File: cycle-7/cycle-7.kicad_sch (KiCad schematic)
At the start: 176 parts, among them J1 Conn_01x06_MountingPin, J2 Conn_01x04_Pin, J3 Conn_01x02_Pin, SW1 SW_Push, U1 XC6206PxxxMR, U2 STM32F401RCTx, Y1 12MHz

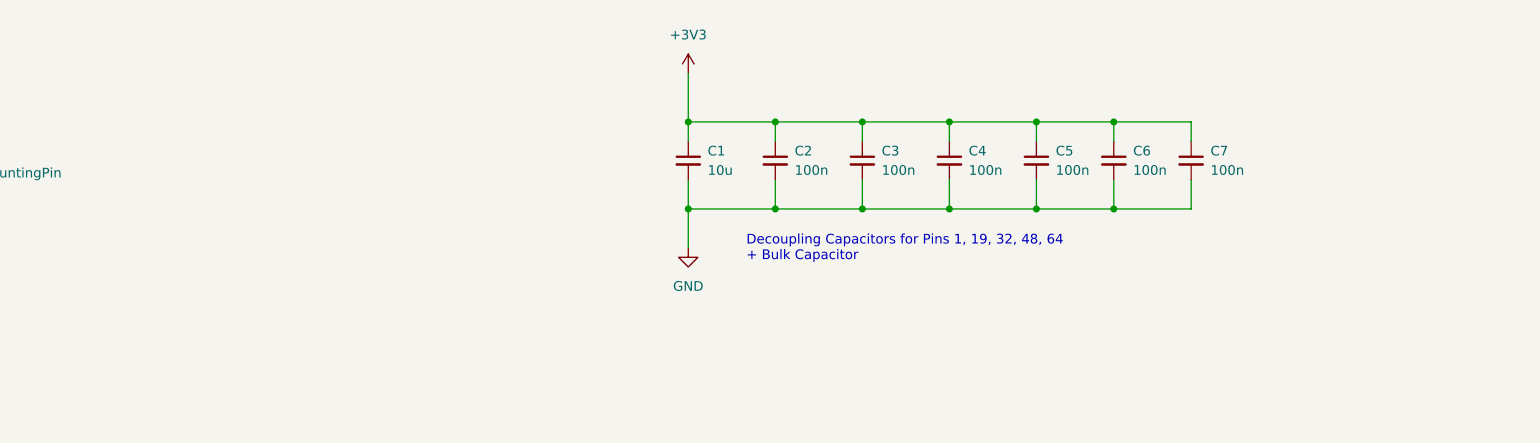
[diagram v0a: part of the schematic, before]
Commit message: fixed layout, added gnd plane stitching
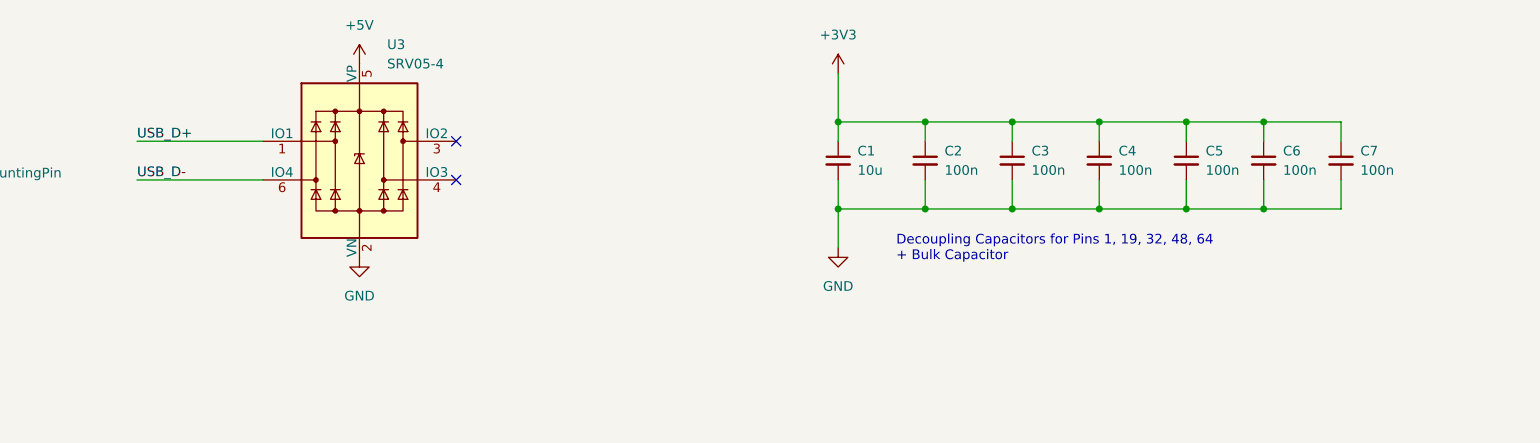
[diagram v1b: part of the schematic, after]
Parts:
- added U3: SRV05-4, PCM_marbastlib-various:SOT-23-6-routable, symbol PCM_marbastlib-various:SRV05-4
- C1, C10, C11, C12, C13, C2, C3, C4, C5, C6, C7, C8, C9: footprint Capacitor_SMD:C_0402_1005Metric -> Capacitor_SMD:C_0603_1608Metric
- D74: footprint LED_SMD:LED_RGB_1210 -> lib-zegonix:SK6812MINI-E_3.2x2.8_reverse_mount
- R1, R2, R3: footprint Resistor_SMD:R_0402_1005Metric -> Resistor_SMD:R_0603_1608Metric
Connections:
- net +5V: now also U3.5 (VP)
- net GND: now also U3.2 (VN)
- net USB_D+: now also U3.1 (IO1)
- net USB_D-: now also U3.6 (IO4)
- no-connect marks 25 -> 27
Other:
- moved on the sheet: C1, C2, C3, C4, C5, C6, C7

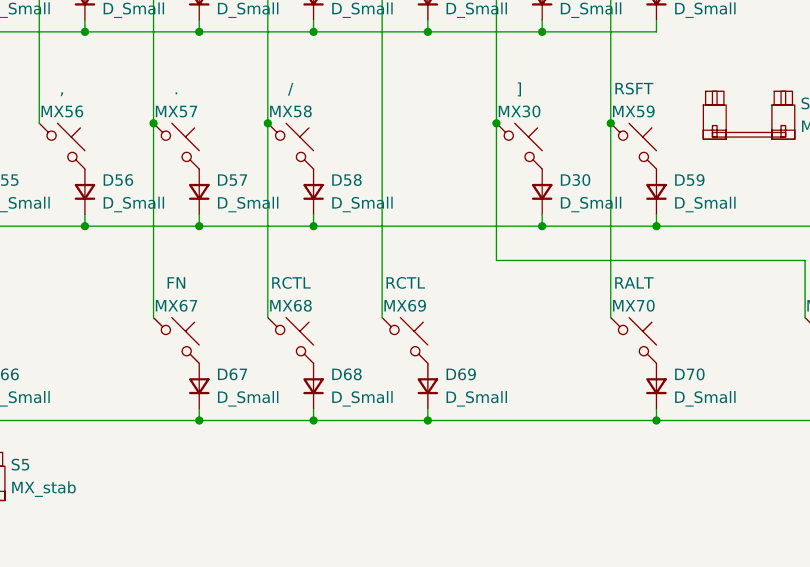
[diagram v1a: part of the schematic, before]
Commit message: added a kicad project for the plate added a kicad project for the daughter board
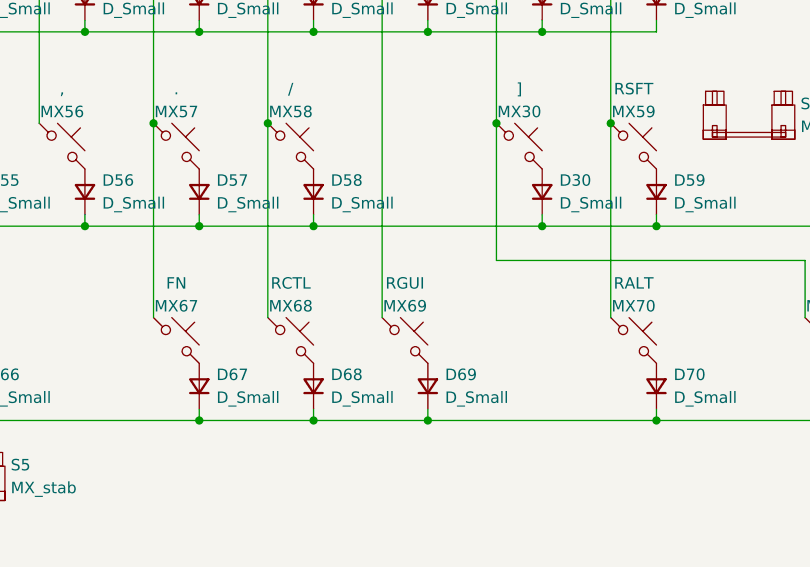
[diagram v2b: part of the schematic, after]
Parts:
- MX69: Key RCTL -> RGUI
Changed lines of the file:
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@@
       (effects (font (size 1.27 1.27)) hide)
     )
-    (property "Key" "RCTL" (at 314.96 195.58 0)
+    (property "Key" "RGUI" (at 314.96 195.58 0)
       (effects (font (size 1.27 1.27)))
     )

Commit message: implemented newest findings from prototype and updated to kicad 8
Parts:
- added R4, R5: 10k, Resistor_SMD:R_0603_1608Metric, symbol Device:R_Small
- C11: value 100n -> 4.7u
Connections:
- net +3V3: now also J3.1 (Pin_1)
- net GND: now also R4.1, R5.1; no longer J3.2 (Pin_2)
- net BOOT1: now reaches U2.28 (PB2)
- net BOOT1: now also R4.2
- net BOOTSEL renamed BOOT0
- net BOOT0: now also J3.2 (Pin_2), R5.2; no longer J3.1 (Pin_1)
- no-connect marks 27 -> 26
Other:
- note removed: "PB2 has alternate Function BOOT1"
- moved on the sheet: C1, C2, C3, C4, C5, C6, C7, D74, J3

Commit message: minor fixes
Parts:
- C11: value 4.7u -> 100n
- renumbered D14 to D13, D15 to D14, D16 to D15, D17 to D16, D18 to D17, D19 to D18, D20 to D19, D21 to D20, D22 to D21, D23 to D22, D24 to D23, D25 to D24, D26 to D25, D27 to D26, D28 to D27, D29 to D28, D31 to D29, D32 to D30, D33 to D31, D34 to D32, D35 to D33, D36 to D34, D37 to D35, D38 to D36, D39 to D37, D40 to D38, D41 to D39, D42 to D40, D43 to D41, D44 to D42, D45 to D43, D46 to D44, D13 to D45, D47 to D46, D48 to D47, D49 to D48, D50 to D49, D51 to D50, D52 to D51, D53 to D52, D54 to D53, D55 to D54, D56 to D55, D57 to D56, D58 to D57, D30 to D58, J3 to J2, J2 to J3, MX14 to MX13, MX15 to MX14, MX16 to MX15, MX17 to MX16, MX18 to MX17, MX19 to MX18, MX20 to MX19, MX21 to MX20, MX22 to MX21, MX23 to MX22, MX24 to MX23, MX25 to MX24, MX26 to MX25, MX27 to MX26, MX28 to MX27, MX29 to MX28, MX31 to MX29, MX32 to MX30, MX33 to MX31, MX34 to MX32, MX35 to MX33, MX36 to MX34, MX37 to MX35, MX38 to MX36, MX39 to MX37, MX40 to MX38, MX41 to MX39, MX42 to MX40, MX43 to MX41, MX44 to MX42, MX45 to MX43, MX46 to MX44, MX13 to MX45, MX47 to MX46, MX48 to MX47, MX49 to MX48, MX50 to MX49, MX51 to MX50, MX52 to MX51, MX53 to MX52, MX54 to MX53, MX55 to MX54, MX56 to MX55, MX57 to MX56, MX58 to MX57, MX30 to MX58, R5 to R4, R4 to R5, S6 to S5, S5 to S6, U3 to U2, U2 to U3

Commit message: added a readme, fixed kicad update mess..
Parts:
- C10: value 100n -> 10n
- J1: footprint Connector_JST:JST_SHL_SM06B-SHLS-TF_1x06-1MP_P1.00mm_Horizontal -> Connector_JST:JST_SH_SM06B-SRSS-TB_1x06-1MP_P1.00mm_Horizontal
- R1, R2: value 27 -> 0
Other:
- note added: "Decoupling Capacitors for Pins 1, 13, 19, 32, 48, 64 + Bulk Capacitor"
- note added: "the F401 chips have the resistors embedded"
- note removed: "Decoupling Capacitors for Pins 1, 19, 32, 48, 64 + Bulk Capacitor"
- moved on the sheet: C10, SW1
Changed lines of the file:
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@@
 	)
 	(junction
-		(at 54.61 49.53)
+		(at 54.61 45.72)
 		(diameter 0)
 		(color 0 0 0 0)
@@
 	(wire
 		(pts
-			(xy 39.37 58.42) (xy 39.37 60.96)
+			(xy 39.37 57.15) (xy 39.37 60.96)
 		)
 		(stroke
@@
 	(wire
 		(pts
-			(xy 39.37 49.53) (xy 54.61 49.53)
+			(xy 39.37 45.72) (xy 54.61 45.72)
 		)
 		(stroke
@@
 	(wire
 		(pts
-			(xy 54.61 49.53) (xy 54.61 50.8)
+			(xy 54.61 45.72) (xy 54.61 49.53)
 		)
 		(stroke
@@
 	(wire
 		(pts
-			(xy 54.61 49.53) (xy 77.47 49.53)
+			(xy 54.61 45.72) (xy 77.47 45.72)
 		)
 		(stroke
@@
 	(wire
 		(pts
+			(xy 54.61 59.69) (xy 54.61 60.96)
+		)
+		(stroke
+			(width 0)
+			(type default)
+		)
+	)
+	(wire
+		(pts
 			(xy 228.6 167.64) (xy 228.6 166.37)
 		)
@@
 	(wire
 		(pts
-			(xy 39.37 49.53) (xy 39.37 53.34)
+			(xy 39.37 45.72) (xy 39.37 52.07)
 		)
 		(stroke
@@
 		)
 	)
-	(text "Decoupling Capacitors for Pins 1, 19, 32, 48, 64\n+ Bulk Capacitor"
+	(text "Decoupling Capacitors for Pins 1, 13, 19, 32, 48, 64\n+ Bulk Capacitor"
 		(exclude_from_sim no)
 		(at 300.355 62.865 0)
@@
 		)
 	)
+	(text "the F401 chips have the resistors embedded"
+		(exclude_from_sim no)
+		(at 118.364 114.3 0)
+		(effects
+			(font
+				(size 1.27 1.27)
+			)
+		)
+	)
 	(label "COL5"
 		(at 236.22 93.98 270)
@@
 	)
 	(label "nRESET"
-		(at 77.47 49.53 180)
+		(at 77.47 45.72 180)
 		(fields_autoplaced yes)
 		(effects
@@
 	(symbol
 		(lib_id "Switch:SW_Push")
-		(at 54.61 55.88 90)
+		(at 54.61 54.61 90)
 		(unit 1)
 		(exclude_from_sim no)
@@
 		(fields_autoplaced yes)
 		(property "Reference" "SW1"
-			(at 56.515 54.61 90)
+			(at 56.515 53.34 90)
 			(effects
 				(font
@@
 		)
 		(property "Value" "SW_Push"
-			(at 56.515 57.15 90)
+			(at 56.515 55.88 90)
 			(effects
 				(font
@@
 		)
 		(property "Footprint" "Button_Switch_SMD:SW_SPST_TL3342"
-			(at 49.53 55.88 0)
+			(at 49.53 54.61 0)
 			(effects
 				(font
@@
 		)
 		(property "Datasheet" "~"
-			(at 49.53 55.88 0)
+			(at 49.53 54.61 0)
 			(effects
 				(font
@@
 		)
 		(property "Description" ""
-			(at 54.61 55.88 0)
+			(at 54.61 54.61 0)
 			(effects
 				(font
@@
 	(symbol
 		(lib_id "Device:C_Small")
-		(at 39.37 55.88 0)
+		(at 39.37 54.61 0)
 		(unit 1)
 		(exclude_from_sim no)
@@
 		(fields_autoplaced yes)
 		(property "Reference" "C10"
-			(at 41.91 54.6163 0)
+			(at 41.91 53.3462 0)
 			(effects
 				(font
@@
 			)
 		)
-		(property "Value" "100n"
-			(at 41.91 57.1563 0)
+		(property "Value" "10n"
+			(at 41.91 55.8862 0)
 			(effects
 				(font
@@
 		)
 		(property "Footprint" "Capacitor_SMD:C_0603_1608Metric"
-			(at 39.37 55.88 0)
+			(at 39.37 54.61 0)
 			(effects
 				(font
@@
 		)
 		(property "Datasheet" "~"
-			(at 39.37 55.88 0)
+			(at 39.37 54.61 0)
 			(effects
 				(font
@@
 		)
 		(property "Description" ""
-			(at 39.37 55.88 0)
+			(at 39.37 54.61 0)
 			(effects
 				(font
@@
 			)
 		)
-		(property "Value" "27"
+		(property "Value" "0"
 			(at 104.775 116.84 90)
 			(effects
@@
 			)
 		)
-		(property "Footprint" "Connector_JST:JST_SHL_SM06B-SHLS-TF_1x06-1MP_P1.00mm_Horizontal"
+		(property "Footprint" "Connector_JST:JST_SH_SM06B-SRSS-TB_1x06-1MP_P1.00mm_Horizontal"
 			(at 165.1 48.26 0)
 			(effects
@@
 			)
 		)
-		(property "Value" "27"
+		(property "Value" "0"
 			(at 104.775 119.38 90)
 			(effects

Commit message: .
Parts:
- added C14: 100n, Capacitor_SMD:C_0603_1608Metric, symbol Device:C_Small
- added R6: 1k, symbol Device:R_Small
- C10: value 10n -> 100n
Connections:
- net +5V: now also C14.1
- net GND: now also C14.2
- net USB_D+: now also U2.3 (IO2)
- net USB_D-: now also U2.4 (IO3)
- net nRESET: now also R6.1; no longer SW1.2
- new net: R6.2, SW1.2
- no-connect marks 26 -> 24
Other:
- moved on the sheet: SW1

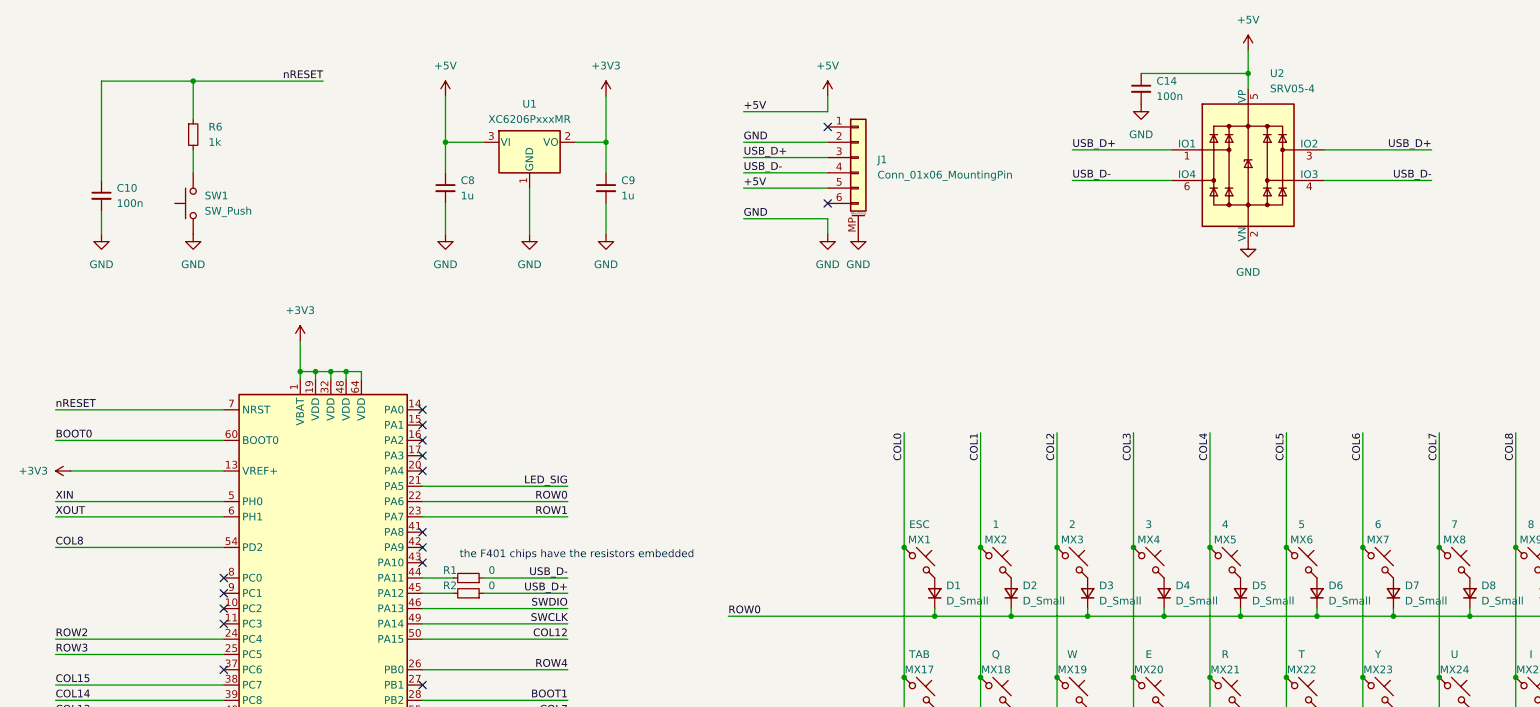
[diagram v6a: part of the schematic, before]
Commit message: updated findings from prototype removed output folder as the vendors stock is everchanging
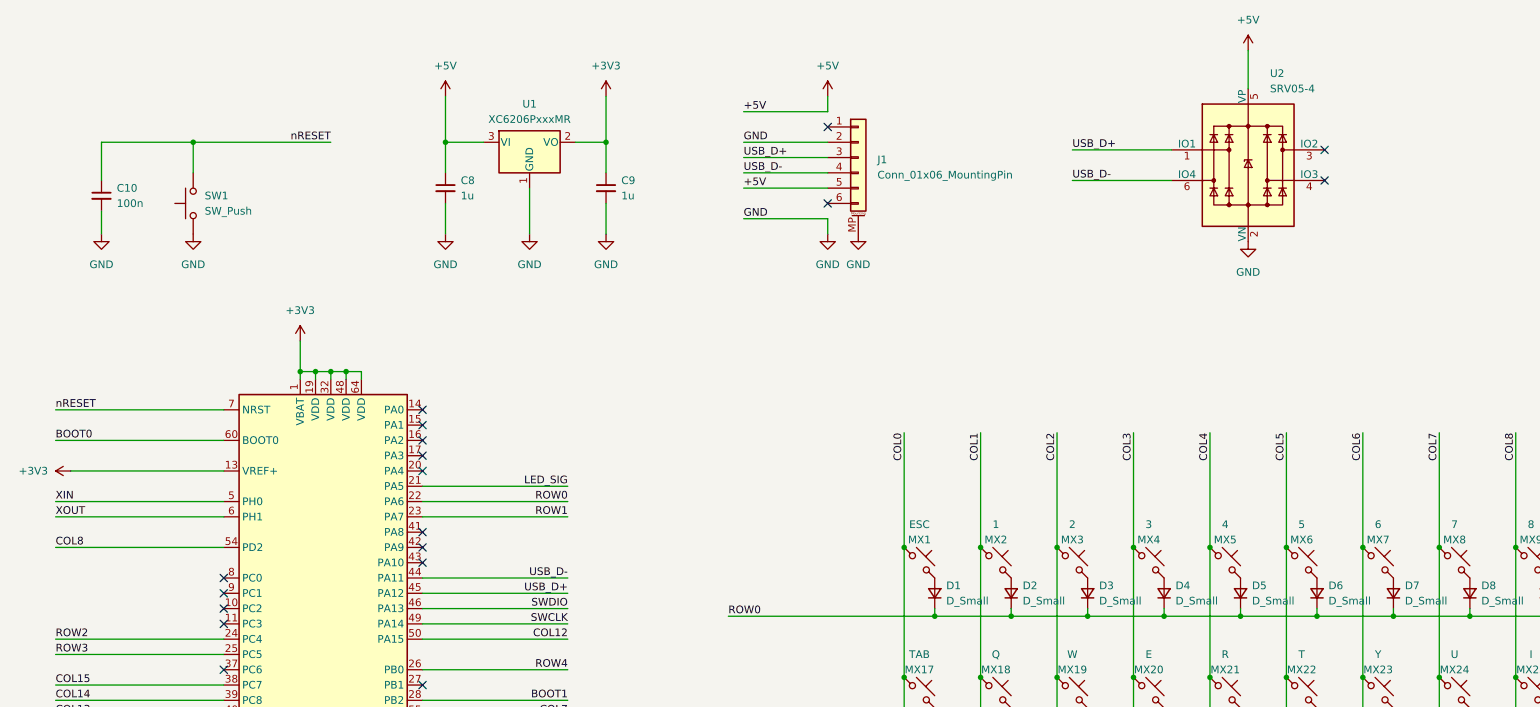
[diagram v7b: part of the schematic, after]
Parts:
- removed C14: 100n, Capacitor_SMD:C_0603_1608Metric, symbol Device:C_Small
- removed R1, R2: 0, Resistor_SMD:R_0603_1608Metric, symbol Device:R_Small
- removed R6: 1k, symbol Device:R_Small
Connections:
- net USB_D+: now also U3.45 (PA12); no longer U2.3 (IO2)
- net USB_D-: now also U3.44 (PA11); no longer U2.4 (IO3)
- net nRESET: now also SW1.2
- no-connect marks 24 -> 26
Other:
- note removed: "the F401 chips have the resistors embedded"
